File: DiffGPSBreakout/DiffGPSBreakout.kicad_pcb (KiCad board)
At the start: 2 copper layers, 110.2 x 72.3 mm, 16 parts, among them U1 Raspberry_Pi

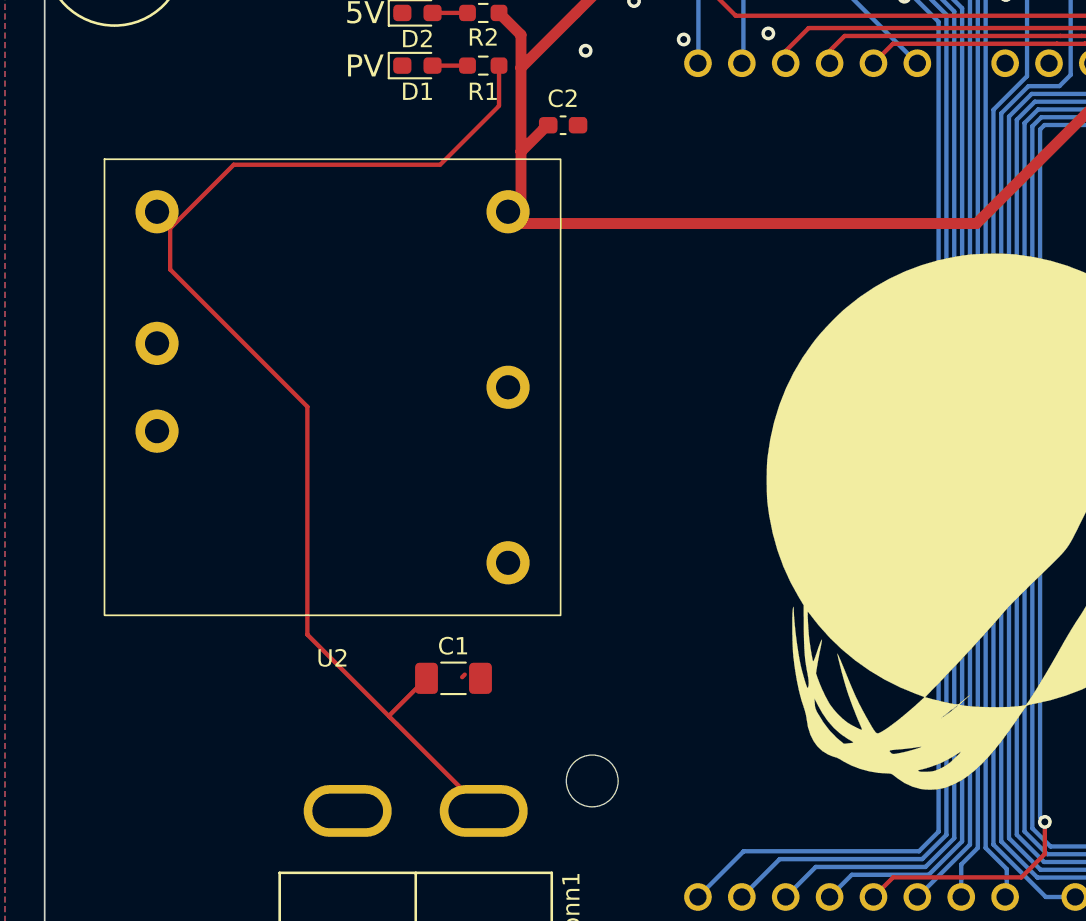
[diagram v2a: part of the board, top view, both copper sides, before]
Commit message: Re-routed traces
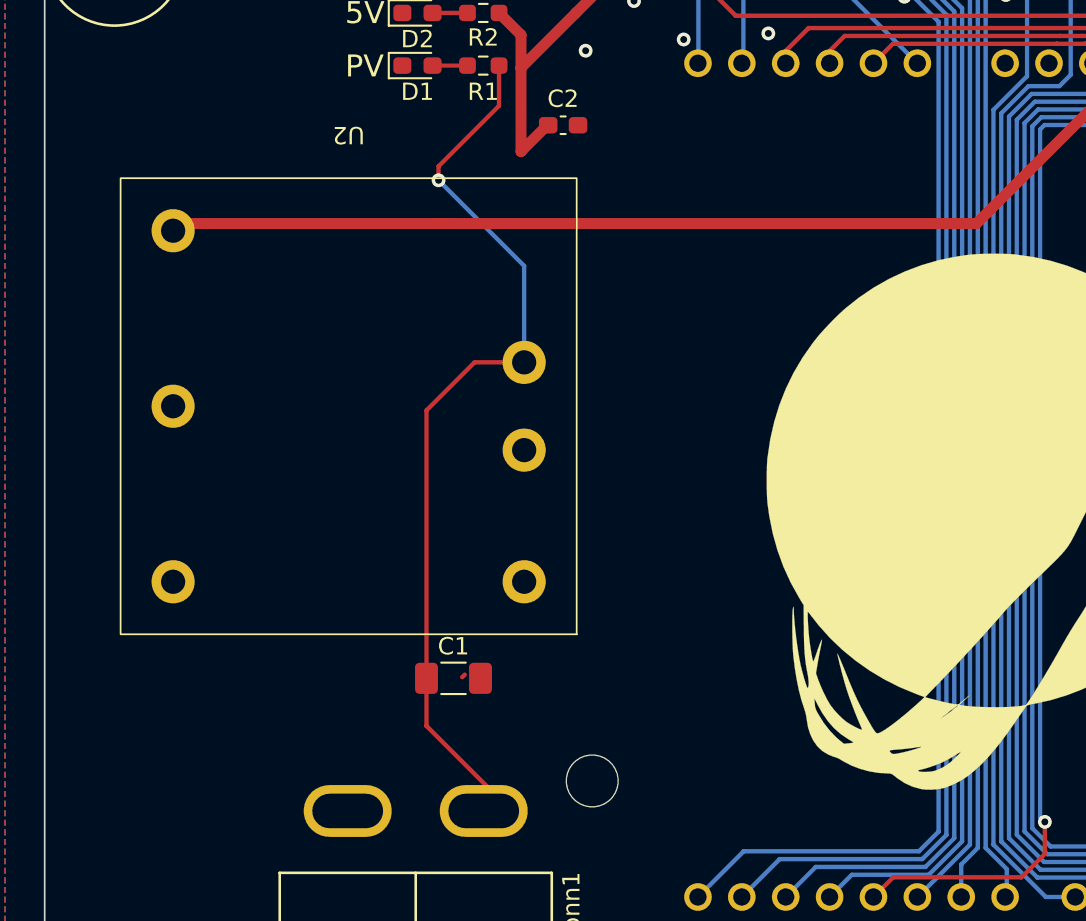
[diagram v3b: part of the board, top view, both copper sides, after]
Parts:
- moved U2 37.2 mm to (114.1, 78.4), turned to 180 degrees
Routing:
- net +5V: track 69.7 -> 86.6 mm
- net VCC: track 69.3 -> 52.7 mm, vias 0 -> 1
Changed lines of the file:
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@@
 	(footprint "MRDT_Devices:PKE3311PI_Through_Hole"
 		(layer "F.Cu")
-		(at 86.734 103.7432)
+		(at 114.065 78.4416 180)
 		(property "Reference" "U2"
-			(at 13.2 2.5 0)
+			(at 13.2 2.5 180)
 			(unlocked yes)
 			(layer "F.SilkS")
@@
 		)
 		(property "Value" "~"
-			(at 14.76 2.45 0)
+			(at 14.76 2.45 180)
 			(unlocked yes)
 			(layer "F.Fab")
@@
 		)
 		(property "Footprint" "MRDT_Devices:PKE3311PI_Through_Hole"
-			(at 13.2 1 0)
+			(at 13.2 1 360)
 			(layer "F.Fab")
 			(hide yes)
@@
 		)
 		(property "Datasheet" ""
-			(at 0 0 0)
+			(at 0 0 360)
 			(layer "F.Fab")
 			(hide yes)
@@
 		)
 		(property "Description" ""
-			(at 0 0 0)
+			(at 0 0 360)
 			(layer "F.Fab")
 			(hide yes)
@@
 		)
 		(fp_text user "${REFERENCE}"
-			(at 13.2 4.35 0)
+			(at 13.2 4.35 180)
 			(unlocked yes)
 			(layer "F.Fab")
@@
 		)
 		(pad "1" thru_hole circle
-			(at 3.04 -23.36)
+			(at 3.04 -23.36 180)
 			(size 2.5 2.5)
 			(drill 1.4)
@@
 		)
 		(pad "2" thru_hole circle
-			(at 3.04 -15.74)
+			(at 3.04 -15.74 180)
 			(size 2.5 2.5)
 			(drill 1.4)
@@
 		)
 		(pad "3" thru_hole circle
-			(at 3.04 -10.66)
+			(at 3.04 -10.66 180)
 			(size 2.5 2.5)
 			(drill 1.4)
@@
 		)
 		(pad "4" thru_hole circle
-			(at 23.36 -3.04)
+			(at 23.36 -3.04 180)
 			(size 2.5 2.5)
 			(drill 1.4)
@@
 		)
 		(pad "5" thru_hole circle
-			(at 23.36 -13.2)
+			(at 23.36 -13.2 180)
 			(size 2.5 2.5)
 			(drill 1.4)
@@
 		)
 		(pad "6" thru_hole circle
-			(at 23.36 -23.36)
+			(at 23.36 -23.36 180)
 			(size 2.5 2.5)
 			(drill 1.4)
@@
 	)
 	(segment
+		(start 146.484119 71.787401)
+		(end 137.206519 81.065001)
+		(width 0.635)
+		(layer "F.Cu")
+		(net 25)
+	)
+	(segment
 		(start 137.206519 81.065001)
-		(end 110.841743 81.065001)
+		(end 91.121599 81.065001)
+		(width 0.635)
+		(layer "F.Cu")
+		(net 25)
+	)
+	(segment
+		(start 91.121599 81.065001)
+		(end 90.705 81.4816)
 		(width 0.635)
 		(layer "F.Cu")
@@
 	)
 	(segment
-		(start 110.841743 70.146525)
-		(end 110.841743 72.053777)
+		(start 105.8672 81.065001)
+		(end 106.676143 81.065001)
 		(width 0.635)
 		(layer "F.Cu")
@@
 	)
 	(segment
-		(start 114.020619 68.874901)
+		(start 110.841743 70.146525)
 		(end 110.841743 72.053777)
 		(width 0.635)
@@
 	)
 	(segment
-		(start 110.841743 76.899401)
-		(end 110.841743 81.065001)
+		(start 114.020619 68.874901)
+		(end 110.841743 72.053777)
 		(width 0.635)
 		(layer "F.Cu")
@@
 	)
 	(segment
-		(start 146.484119 71.787401)
-		(end 137.206519 81.065001)
-		(width 0.635)
-		(layer "F.Cu")
-		(net 25)
-	)
-	(segment
 		(start 154.763547 70.660401)
 		(end 143.484413 70.660401)
@@
 	)
 	(segment
-		(start 98.4758 104.858882)
-		(end 103.251219 109.634301)
-		(width 0.25)
-		(layer "F.Cu")
-		(net 31)
-	)
-	(segment
-		(start 108.935119 115.318201)
-		(end 103.6396 110.022682)
+		(start 105.3715 110.1467)
+		(end 105.3715 107.3912)
 		(width 0.254)
 		(layer "F.Cu")
@@
 	)
 	(segment
-		(start 90.534 81.3432)
-		(end 90.534 83.7268)
+		(start 106.0704 77.75112)
+		(end 106.0704 78.5622)
 		(width 0.25)
 		(layer "F.Cu")
@@
 	)
 	(segment
-		(start 98.4758 91.6686)
-		(end 98.4758 104.858882)
+		(start 111.025 89.1016)
+		(end 108.1548 89.1016)
 		(width 0.25)
 		(layer "F.Cu")
@@
 	)
 	(segment
-		(start 109.570119 74.251401)
-		(end 106.159119 77.662401)
-		(width 0.25)
-		(layer "F.Cu")
-		(net 31)
-	)
-	(segment
-		(start 94.214799 77.662401)
-		(end 90.534 81.3432)
+		(start 109.534119 71.958901)
+		(end 109.570119 71.922901)
 		(width 0.254)
 		(layer "F.Cu")
@@
 	)
 	(segment
-		(start 105.3715 107.3912)
-		(end 103.251219 109.511481)
+		(start 107.434901 107.325481)
+		(end 107.587301 107.173081)
 		(width 0.25)
 		(layer "F.Cu")
@@
 	)
 	(segment
-		(start 103.251219 109.511481)
-		(end 103.251219 109.634301)
-		(width 0.25)
+		(start 108.935119 113.710319)
+		(end 105.3715 110.1467)
+		(width 0.254)
 		(layer "F.Cu")
 		(net 31)
 	)
 	(segment
-		(start 109.534119 71.958901)
-		(end 109.570119 71.922901)
+		(start 108.935119 115.318201)
+		(end 108.935119 113.710319)
 		(width 0.254)
 		(layer "F.Cu")
@@
 	)
 	(segment
-		(start 107.434901 107.325481)
-		(end 107.587301 107.173081)
+		(start 105.3715 91.8849)
+		(end 105.3715 107.3912)
 		(width 0.25)
 		(layer "F.Cu")
@@
 	)
 	(segment
-		(start 90.534 83.7268)
-		(end 98.4758 91.6686)
+		(start 108.1548 89.1016)
+		(end 105.3715 91.8849)
 		(width 0.25)
 		(layer "F.Cu")
@@
 	)
 	(segment
-		(start 103.251219 109.634301)
-		(end 103.6396 110.022682)
+		(start 109.570119 74.251401)
+		(end 106.0704 77.75112)
 		(width 0.25)
 		(layer "F.Cu")
 		(net 31)
 	)
+	(via
+		(at 106.0704 78.5622)
+		(size 0.8)
+		(drill 0.4)
+		(layers "F.Cu" "B.Cu")
+		(net 31)
+	)
 	(segment
-		(start 106.159119 77.662401)
-		(end 94.214799 77.662401)
-		(width 0.254)
-		(layer "F.Cu")
+		(start 111.025 83.5168)
+		(end 111.025 89.1016)
+		(width 0.25)
+		(layer "B.Cu")
+		(net 31)
+	)
+	(segment
+		(start 106.0704 78.5622)
+		(end 111.025 83.5168)
+		(width 0.25)
+		(layer "B.Cu")
 		(net 31)
 	)

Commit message: Fixed traces pt.2
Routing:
- net +5V: track 86.6 -> 92.7 mm
- net VCC: track 52.7 -> 51.6 mm
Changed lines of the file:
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@@
 	)
 	(segment
-		(start 137.206519 81.065001)
-		(end 91.121599 81.065001)
+		(start 115.007343 81.065001)
+		(end 115.189 81.065001)
 		(width 0.635)
 		(layer "F.Cu")
@@
 	)
 	(segment
+		(start 137.206519 81.065001)
+		(end 115.189 81.065001)
+		(width 0.635)
+		(layer "F.Cu")
+		(net 25)
+	)
+	(segment
+		(start 115.189 81.065001)
+		(end 91.121599 81.065001)
+		(width 0.635)
+		(layer "F.Cu")
+		(net 25)
+	)
+	(segment
 		(start 105.8672 81.065001)
 		(end 106.676143 81.065001)
@@
 		(start 112.365743 75.375401)
 		(end 110.841743 76.899401)
+		(width 0.635)
+		(layer "F.Cu")
+		(net 25)
+	)
+	(segment
+		(start 110.841743 76.899401)
+		(end 115.007343 81.065001)
 		(width 0.635)
 		(layer "F.Cu")
@@
 	)
 	(segment
-		(start 106.0704 77.75112)
-		(end 106.0704 78.5622)
-		(width 0.25)
-		(layer "F.Cu")
-		(net 31)
-	)
-	(segment
-		(start 109.570119 71.922901)
+		(start 107.32856 76.49296)
 		(end 109.570119 74.251401)
+		(width 0.25)
+		(layer "F.Cu")
+		(net 31)
+	)
+	(segment
+		(start 109.570119 74.251401)
+		(end 109.570119 71.922901)
 		(width 0.25)
 		(layer "F.Cu")
@@
 		(net 31)
 	)
-	(segment
-		(start 109.570119 74.251401)
-		(end 106.0704 77.75112)
-		(width 0.25)
-		(layer "F.Cu")
-		(net 31)
-	)
 	(via
-		(at 106.0704 78.5622)
+		(at 107.32856 76.49296)
 		(size 0.8)
 		(drill 0.4)
@@
 	)
 	(segment
+		(start 107.32856 79.82036)
+		(end 111.025 83.5168)
+		(width 0.25)
+		(layer "B.Cu")
+		(net 31)
+	)
+	(segment
 		(start 111.025 83.5168)
 		(end 111.025 89.1016)
@@
 	)
 	(segment
-		(start 106.0704 78.5622)
-		(end 111.025 83.5168)
-		(width 0.25)
-		(layer "B.Cu")
+		(start 107.32856 76.49296)
+		(end 107.32856 79.82036)
+		(width 0.25)
+		(layer "B.Cu")
